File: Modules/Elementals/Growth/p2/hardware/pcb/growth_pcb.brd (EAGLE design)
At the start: 17.8 x 101.9 mm, 22 parts, among them J1 EURO_POWER, J2 WQP-PJ398SM6, J3 WQP-PJ398SM6, J4 WQP-PJ398SM6, J5 WQP-PJ398SM6, U1 TL072P

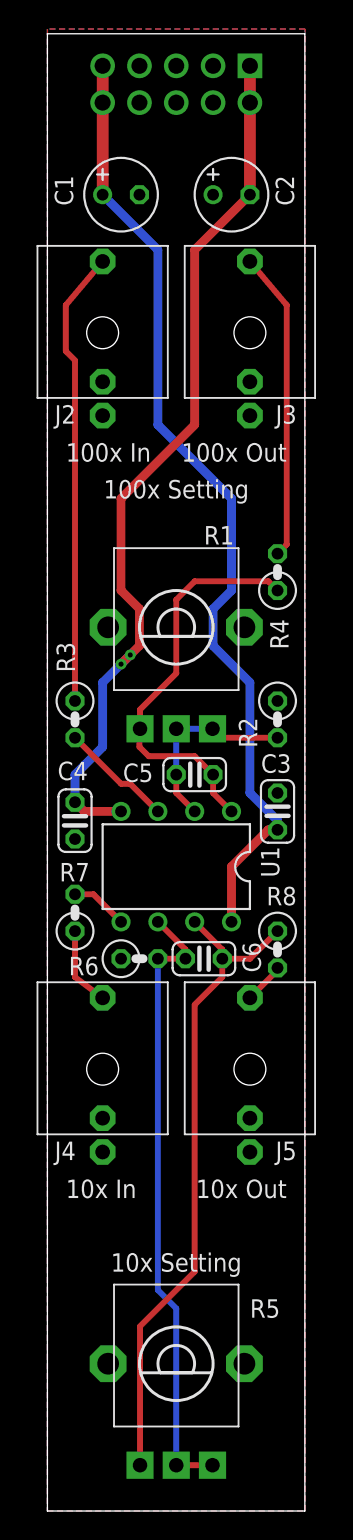
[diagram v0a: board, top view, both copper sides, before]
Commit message: New standard power input block on Growth V2
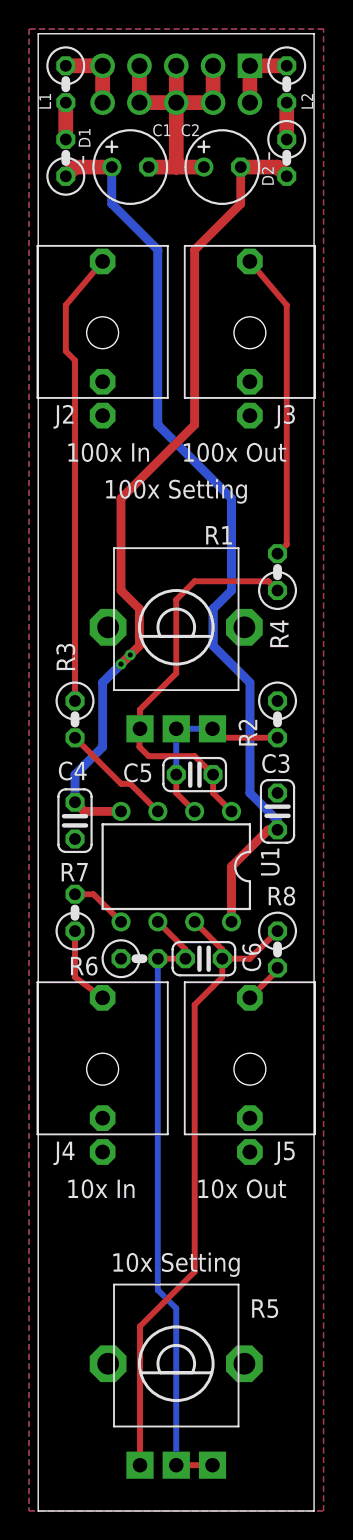
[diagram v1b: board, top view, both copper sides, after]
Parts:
- added D1, D2: SB230TA, SonicAthame:0207/2V-POL
- added L1, L2: 2743005112, SonicAthame:0207/2V
- moved C1 2.01 mm to (6.99, 103.5)
- moved C2 2.01 mm to (13.3, 103.5)
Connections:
- new net N$15: D1.A, L1.2
- new net N$16: D2.C, L2.2
- new net N$17: J1.1, J1.10, L2.1
- new net N$18: J1.5, J1.6, L1.1
- net +12V: now also D1.C; no longer J1.5, J1.6
- net -12V: now also D2.A; no longer J1.1, J1.10
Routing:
- net GND: track 0.00 -> 21.0 mm
- net N$17: track 0.00 -> 5.08 mm
- net N$18: track 0.00 -> 5.08 mm
- net +12V: track 66.8 -> 63.0 mm
- net -12V: track 61.2 -> 57.4 mm
- net N$16: track 0.00 -> 2.54 mm
- net N$15: track 0.00 -> 2.54 mm
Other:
- board size 17.8 x 101.9 mm -> 19 x 101.9 mm
- board text added: "STRIPE"

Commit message: Finished elemental growth p2 PCB
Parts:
- U1: value TL072P -> LM4562NA
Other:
- board text added: "Sonic Athame is fully open-hardware and open-software! Find schematics, code, ans assembly instructions at sonic-athame.com"
- board text removed: "Sonic Athame is fully open-hardware and open-software! Find schematics and code on the official GitHub: github.com/nimaid/Sonic-Athame-eurorack"
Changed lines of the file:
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@@
 </layers>
 <board>
-<fusionsync huburn="a.cGVyc29uYWw6dWUyZGY0M2Ex" projecturn="a.cGVyc29uYWw6dWUyZGY0M2ExIzIwMjAwODA5MzIyMjM2MzA2" f3durn="urn:adsk.wipprod:dm.lineage:43Y-leHDTHinlHHPKq_Q3A" pcbguid="f53b1eb7-f480-46a5-9735-94fbd804d7ef" lastpulledtime="" lastsyncedchangeguid="98395930-98b6-93c1-0850-5e7e071cf0c9" latestrevisionid="" lastsyncedrevisionid="" lastboardhashguid="64b547dd-6a4c-b4b2-7d88-0f9c14c84f44" lastpushedtime="2021-01-28T04:19:03Z" linktopcb3d="false"/>
+<fusionsync huburn="a.cGVyc29uYWw6dWUyZGY0M2Ex" projecturn="a.cGVyc29uYWw6dWUyZGY0M2ExIzIwMjAwODA5MzIyMjM2MzA2" f3durn="urn:adsk.wipprod:dm.lineage:43Y-leHDTHinlHHPKq_Q3A" pcbguid="f53b1eb7-f480-46a5-9735-94fbd804d7ef" lastpulledtime="" lastsyncedchangeguid="98395930-98b6-93c1-0850-5e7e071cf0c9" latestrevisionid="" lastsyncedrevisionid="" lastboardhashguid="358cd26d-b0ab-f703-a2be-fe463827a6a1" lastpushedtime="2021-01-28T17:59:34Z" linktopcb3d="false"/>
 <plain>
 <wire x1="0.635" y1="10.795" x2="19.665" y2="10.795" width="0" layer="20"/>
@@
 <text x="10.16" y="27.305" size="1.27" layer="25" align="bottom-center">10x Setting</text>
 <text x="10.16" y="24.765" size="1.27" layer="26" rot="MR0" align="center">Elemental Growth</text>
-<text x="10.16" y="88.265" size="0.8128" layer="26" rot="MR270" align="center">Sonic Athame is fully open-hardware
-and open-software! Find schematics
-and code on the official GitHub:
-github.com/nimaid/Sonic-Athame-eurorack</text>
+<text x="10.16" y="88.265" size="1.016" layer="26" rot="MR270" align="center">Sonic Athame is fully open-hardware
+and open-software! Find schematics,
+code, ans assembly instructions at
+sonic-athame.com</text>
 <text x="10.16" y="17.145" size="1.778" layer="26" rot="MR0" align="center">Prototype v2</text>
 <text x="18.669" y="109.22" size="0.6096" layer="26" rot="MR90" align="bottom-center">STRIPE</text>
@@
 </autorouter>
 <elements>
-<element name="U1" library="SonicAthame" library_urn="urn:adsk.eagle:library:22327399" package="DIL08" package3d_urn="urn:adsk.eagle:package:16409/2" value="TL072P" x="10.16" y="55.245" smashed="yes" rot="R180">
+<element name="U1" library="SonicAthame" library_urn="urn:adsk.eagle:library:22327399" package="DIL08" package3d_urn="urn:adsk.eagle:package:16409/2" value="LM4562NA" x="10.16" y="55.245" smashed="yes" rot="R180">
 <attribute name="NAME" x="16.002" y="56.642" size="1.27" layer="25" ratio="10" rot="R270"/>
 <attribute name="POPULARITY" value="13" x="10.16" y="55.245" size="1.778" layer="27" rot="R180" display="off"/>
